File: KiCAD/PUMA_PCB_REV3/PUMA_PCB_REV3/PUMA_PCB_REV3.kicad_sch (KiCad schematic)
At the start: 17 parts, among them J1 87832-0411, J2 CONMHF1-SMD-G-T, J3 CONMHF1-SMD-G-T, U1 MICROFC-30035-SMT-TR1, U2 MICROFC-30035-SMT-TR1

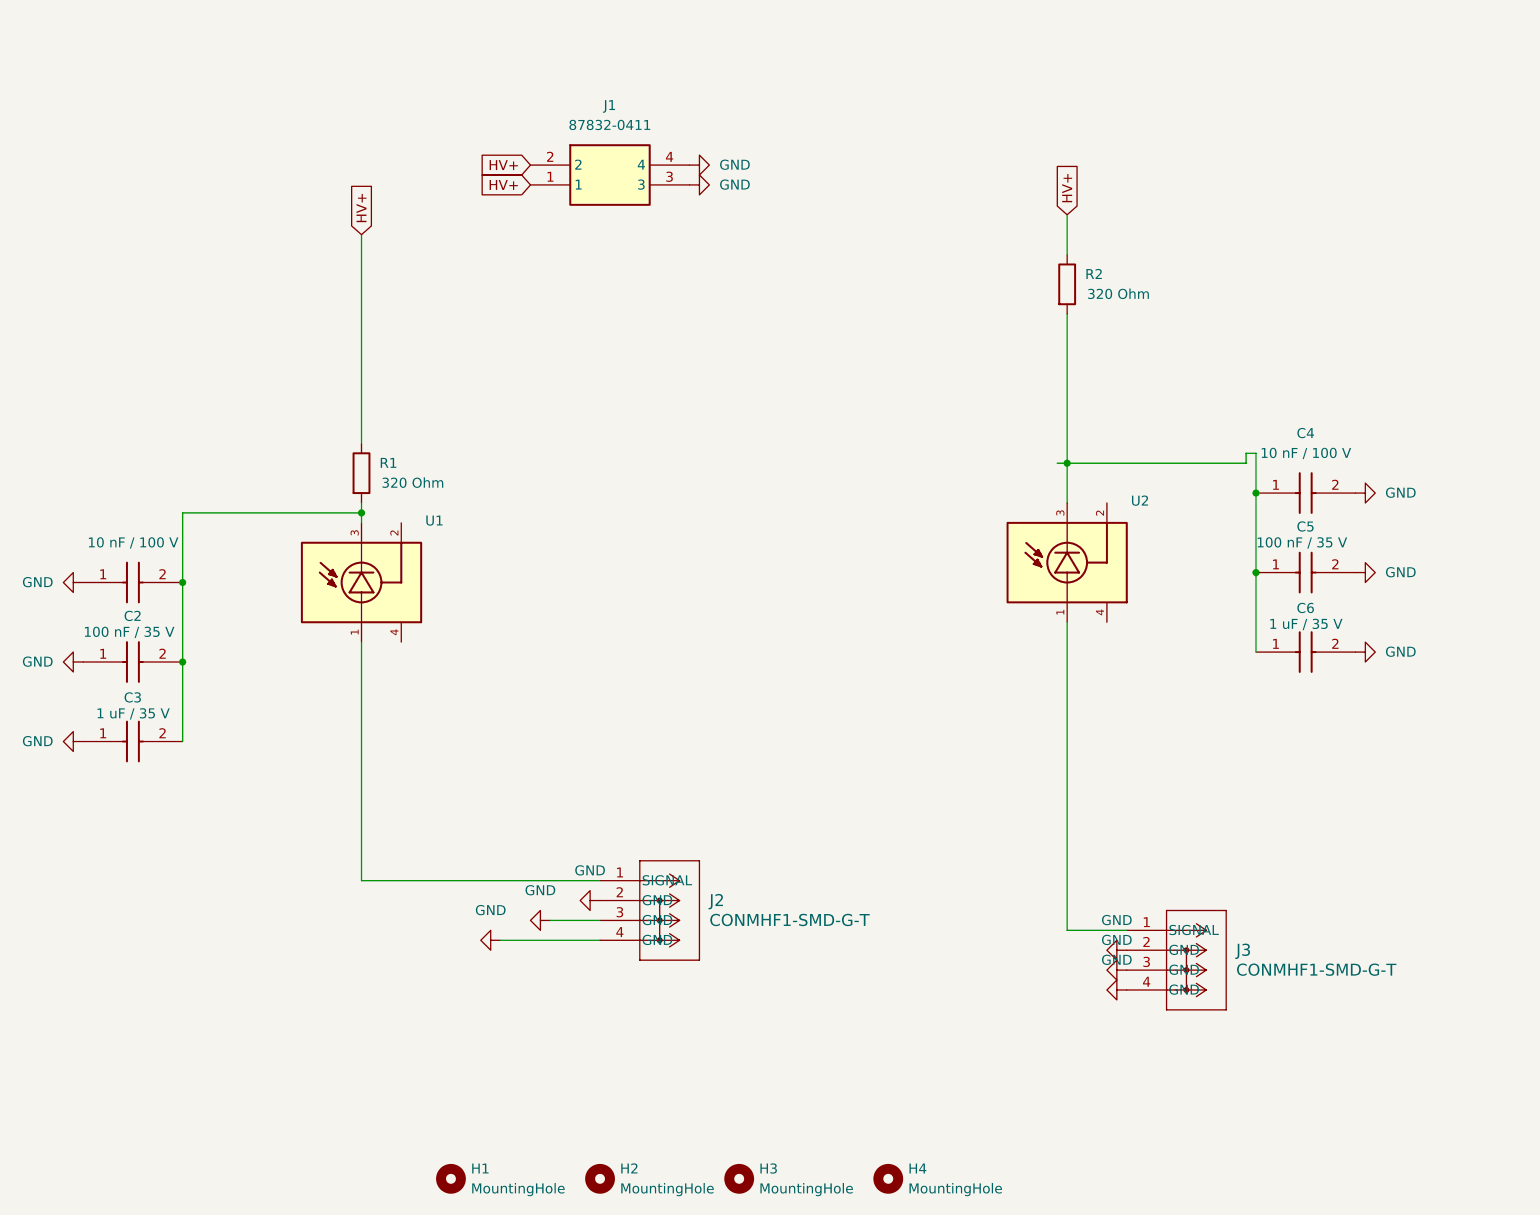
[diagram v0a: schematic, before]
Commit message: new rev 3, since one of the mounting holes was broken
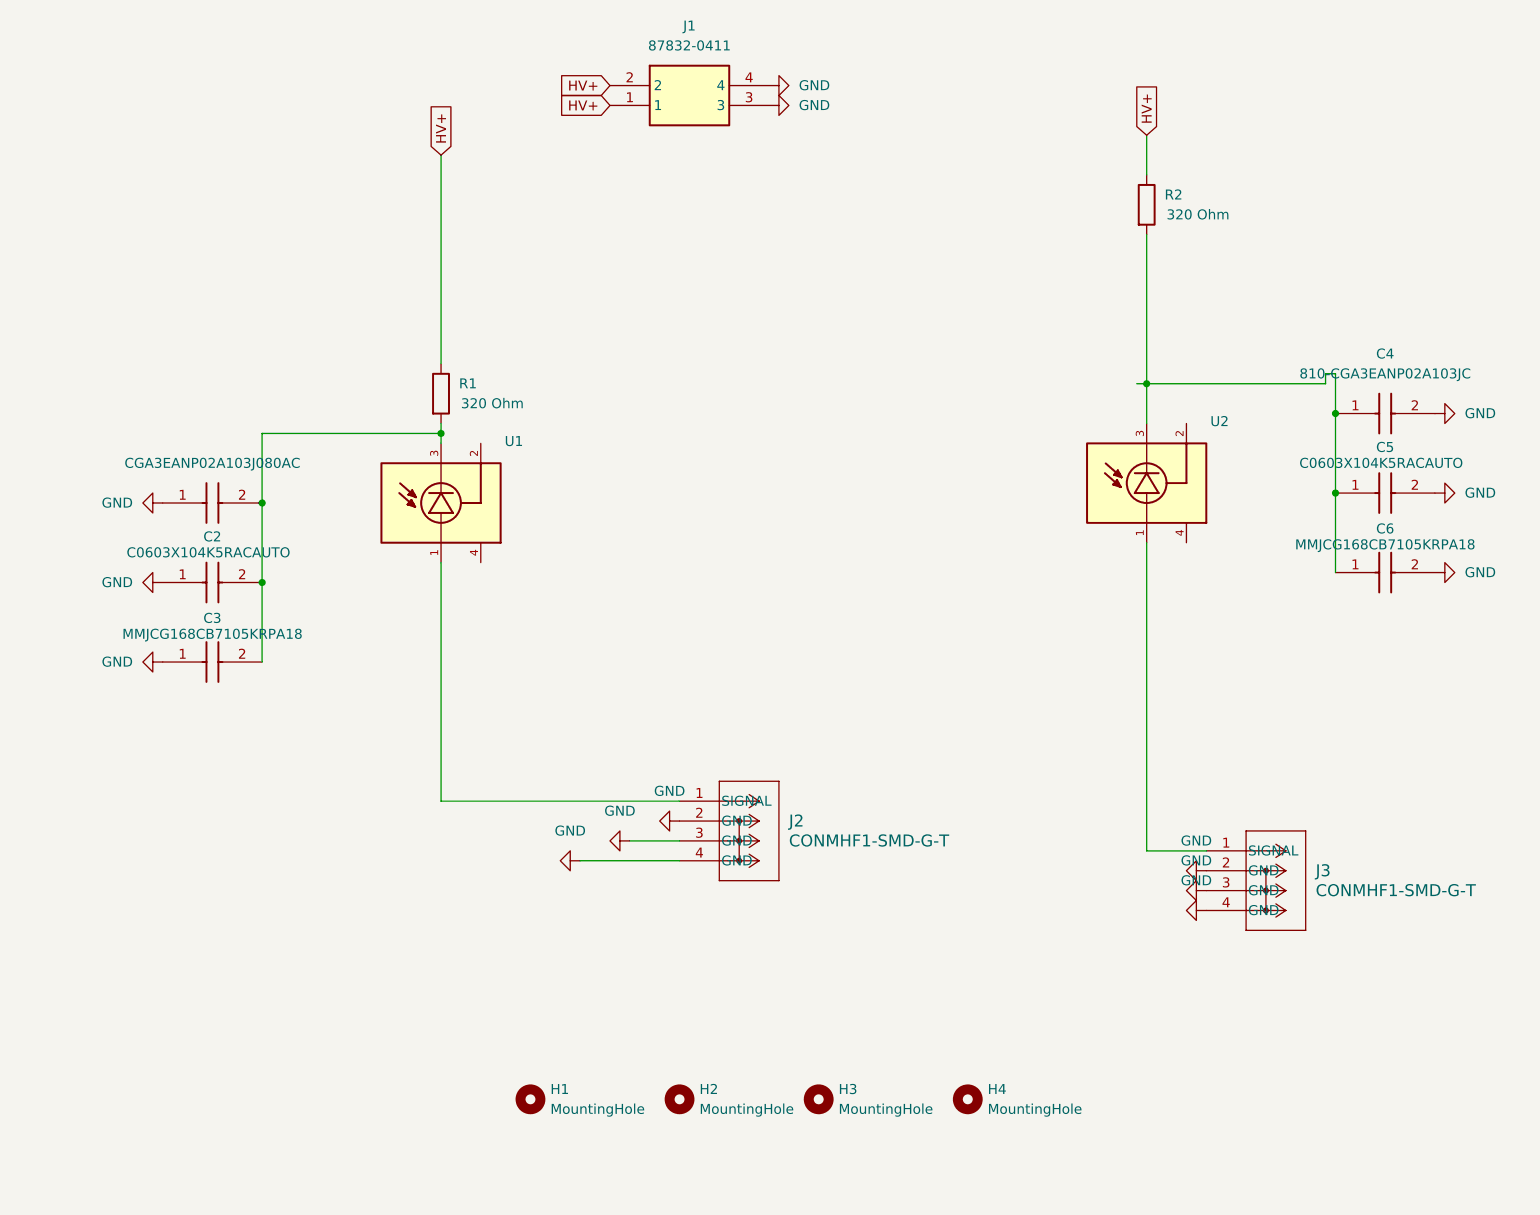
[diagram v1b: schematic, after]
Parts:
- C1: value 10 nF / 100 V -> CGA3EANP02A103J080AC; footprint CAPC1608X90N -> Capacitor_SMD:C_0603_1608Metric_Pad1.08x0.95mm_HandSolder
- C2: value 100 nF / 35 V -> C0603X104K5RACAUTO; footprint CAPC1608X90N -> Capacitor_SMD:C_0603_1608Metric_Pad1.08x0.95mm_HandSolder
- C3, C6: value 1 uF / 35 V -> MMJCG168CB7105KRPA18; footprint CAPC1608X90N -> Capacitor_SMD:C_0603_1608Metric_Pad1.08x0.95mm_HandSolder
- C4: value 10 nF / 100 V -> 810-CGA3EANP02A103JC; footprint CAPC1608X90N -> Capacitor_SMD:C_0603_1608Metric_Pad1.08x0.95mm_HandSolder
- C5: value 100 nF / 35 V -> C0603X104K5RACAUTO; footprint CAPC1608X90N -> Capacitor_SMD:C_0603_1608Metric_Pad1.08x0.95mm_HandSolder; Mouser Part Number 810-CGA3EANP02A103JC -> C0603X104K5RACAUTO
- R1, R2: footprint Resistor_SMD:R_0201_0603Metric -> Resistor_SMD:R_0603_1608Metric_Pad0.98x0.95mm_HandSolder
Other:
- title: PUMA_PCB_REV2 -> (none)
